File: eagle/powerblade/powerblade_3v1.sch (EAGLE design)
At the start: 94 parts, among them J1 JTAG_14PIN_IDC-NL, J21 AC_INSLOT2, J4 TC2030-JLINK-NL, Q1 2N7002, Q3 2SK1829, Q4 2SK1829, U1 TPS62122, U2 MCP6V3, U3 MSP430FR5738, U4 NRF51822QF, U6 MAX9910, U7 OPA2369, X1 16MHz, X3 32.768kHz, Y1 UREACH_XTEND

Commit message: 25 airwires
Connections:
- net GND2: now also U4.P27/AIN1/XL1
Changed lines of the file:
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@@
 <grid distance="0.1" unitdist="inch" unit="inch" style="lines" multiple="1" display="no" altdistance="0.01" altunitdist="inch" altunit="inch"/>
 <layers>
-<layer number="1" name="Top" color="4" fill="1" visible="yes" active="no"/>
-<layer number="2" name="Route2" color="1" fill="3" visible="yes" active="no"/>
-<layer number="3" name="Route3" color="4" fill="3" visible="yes" active="no"/>
-<layer number="4" name="Route4" color="1" fill="4" visible="yes" active="no"/>
-<layer number="5" name="Route5" color="4" fill="4" visible="yes" active="no"/>
-<layer number="6" name="Route6" color="1" fill="8" visible="yes" active="no"/>
-<layer number="7" name="Route7" color="4" fill="8" visible="yes" active="no"/>
-<layer number="8" name="Route8" color="1" fill="2" visible="yes" active="no"/>
-<layer number="9" name="Route9" color="4" fill="2" visible="yes" active="no"/>
-<layer number="10" name="Route10" color="1" fill="7" visible="yes" active="no"/>
-<layer number="11" name="Route11" color="4" fill="7" visible="yes" active="no"/>
-<layer number="12" name="Route12" color="1" fill="5" visible="yes" active="no"/>
-<layer number="13" name="Route13" color="4" fill="5" visible="yes" active="no"/>
-<layer number="14" name="Route14" color="1" fill="6" visible="yes" active="no"/>
-<layer number="15" name="Route15" color="4" fill="6" visible="yes" active="no"/>
-<layer number="16" name="Bottom" color="1" fill="1" visible="yes" active="no"/>
-<layer number="17" name="Pads" color="2" fill="1" visible="yes" active="no"/>
-<layer number="18" name="Vias" color="2" fill="1" visible="yes" active="no"/>
-<layer number="19" name="Unrouted" color="6" fill="1" visible="yes" active="no"/>
-<layer number="20" name="Dimension" color="15" fill="1" visible="yes" active="no"/>
-<layer number="21" name="tPlace" color="7" fill="1" visible="yes" active="no"/>
-<layer number="22" name="bPlace" color="7" fill="1" visible="yes" active="no"/>
-<layer number="23" name="tOrigins" color="15" fill="1" visible="yes" active="no"/>
-<layer number="24" name="bOrigins" color="15" fill="1" visible="yes" active="no"/>
-<layer number="25" name="tNames" color="7" fill="1" visible="yes" active="no"/>
-<layer number="26" name="bNames" color="7" fill="1" visible="yes" active="no"/>
-<layer number="27" name="tValues" color="7" fill="1" visible="yes" active="no"/>
-<layer number="28" name="bValues" color="7" fill="1" visible="yes" active="no"/>
+<layer number="1" name="Top" color="4" fill="1" visible="no" active="no"/>
+<layer number="2" name="Route2" color="1" fill="3" visible="no" active="no"/>
+<layer number="3" name="Route3" color="4" fill="3" visible="no" active="no"/>
+<layer number="4" name="Route4" color="1" fill="4" visible="no" active="no"/>
+<layer number="5" name="Route5" color="4" fill="4" visible="no" active="no"/>
+<layer number="6" name="Route6" color="1" fill="8" visible="no" active="no"/>
+<layer number="7" name="Route7" color="4" fill="8" visible="no" active="no"/>
+<layer number="8" name="Route8" color="1" fill="2" visible="no" active="no"/>
+<layer number="9" name="Route9" color="4" fill="2" visible="no" active="no"/>
+<layer number="10" name="Route10" color="1" fill="7" visible="no" active="no"/>
+<layer number="11" name="Route11" color="4" fill="7" visible="no" active="no"/>
+<layer number="12" name="Route12" color="1" fill="5" visible="no" active="no"/>
+<layer number="13" name="Route13" color="4" fill="5" visible="no" active="no"/>
+<layer number="14" name="Route14" color="1" fill="6" visible="no" active="no"/>
+<layer number="15" name="Route15" color="4" fill="6" visible="no" active="no"/>
+<layer number="16" name="Bottom" color="1" fill="1" visible="no" active="no"/>
+<layer number="17" name="Pads" color="2" fill="1" visible="no" active="no"/>
+<layer number="18" name="Vias" color="2" fill="1" visible="no" active="no"/>
+<layer number="19" name="Unrouted" color="6" fill="1" visible="no" active="no"/>
+<layer number="20" name="Dimension" color="15" fill="1" visible="no" active="no"/>
+<layer number="21" name="tPlace" color="7" fill="1" visible="no" active="no"/>
+<layer number="22" name="bPlace" color="7" fill="1" visible="no" active="no"/>
+<layer number="23" name="tOrigins" color="15" fill="1" visible="no" active="no"/>
+<layer number="24" name="bOrigins" color="15" fill="1" visible="no" active="no"/>
+<layer number="25" name="tNames" color="7" fill="1" visible="no" active="no"/>
+<layer number="26" name="bNames" color="7" fill="1" visible="no" active="no"/>
+<layer number="27" name="tValues" color="7" fill="1" visible="no" active="no"/>
+<layer number="28" name="bValues" color="7" fill="1" visible="no" active="no"/>
 <layer number="29" name="tStop" color="7" fill="3" visible="no" active="no"/>
 <layer number="30" name="bStop" color="7" fill="6" visible="no" active="no"/>
@@
 <layer number="35" name="tGlue" color="7" fill="4" visible="no" active="no"/>
 <layer number="36" name="bGlue" color="7" fill="5" visible="no" active="no"/>
-<layer number="37" name="tTest" color="7" fill="1" visible="yes" active="no"/>
-<layer number="38" name="bTest" color="7" fill="1" visible="yes" active="no"/>
+<layer number="37" name="tTest" color="7" fill="1" visible="no" active="no"/>
+<layer number="38" name="bTest" color="7" fill="1" visible="no" active="no"/>
 <layer number="39" name="tKeepout" color="4" fill="11" visible="no" active="no"/>
 <layer number="40" name="bKeepout" color="1" fill="11" visible="no" active="no"/>
@@
 <layer number="44" name="Drills" color="7" fill="1" visible="no" active="no"/>
 <layer number="45" name="Holes" color="7" fill="1" visible="no" active="no"/>
-<layer number="46" name="Milling" color="3" fill="1" visible="yes" active="no"/>
-<layer number="47" name="Measures" color="7" fill="1" visible="yes" active="no"/>
-<layer number="48" name="Document" color="7" fill="1" visible="yes" active="no"/>
-<layer number="49" name="Reference" color="7" fill="1" visible="yes" active="no"/>
-<layer number="50" name="dxf" color="7" fill="1" visible="yes" active="no"/>
-<layer number="51" name="tDocu" color="7" fill="1" visible="yes" active="no"/>
-<layer number="52" name="bDocu" color="7" fill="1" visible="yes" active="no"/>
-<layer number="53" name="tGND_GNDA" color="7" fill="9" visible="yes" active="no"/>
-<layer number="54" name="bGND_GNDA" color="1" fill="9" visible="yes" active="no"/>
-<layer number="56" name="wert" color="7" fill="1" visible="yes" active="no"/>
-<layer number="57" name="tCAD" color="7" fill="1" visible="yes" active="no"/>
+<layer number="46" name="Milling" color="3" fill="1" visible="no" active="no"/>
+<layer number="47" name="Measures" color="7" fill="1" visible="no" active="no"/>
+<layer number="48" name="Document" color="7" fill="1" visible="no" active="no"/>
+<layer number="49" name="Reference" color="7" fill="1" visible="no" active="no"/>
+<layer number="50" name="dxf" color="7" fill="1" visible="no" active="no"/>
+<layer number="51" name="tDocu" color="7" fill="1" visible="no" active="no"/>
+<layer number="52" name="bDocu" color="7" fill="1" visible="no" active="no"/>
+<layer number="53" name="tGND_GNDA" color="7" fill="9" visible="no" active="no"/>
+<layer number="54" name="bGND_GNDA" color="1" fill="9" visible="no" active="no"/>
+<layer number="56" name="wert" color="7" fill="1" visible="no" active="no"/>
+<layer number="57" name="tCAD" color="7" fill="1" visible="no" active="no"/>
 <layer number="91" name="Nets" color="2" fill="1" visible="yes" active="yes"/>
 <layer number="92" name="Busses" color="1" fill="1" visible="yes" active="yes"/>
@@
 <attribute name="DIGIKEY" value="445-5947-1-ND"/>
 </part>
+<part name="SUPPLY9" library="supply2" deviceset="GND2" device=""/>
 </parts>
 <sheets>
@@
 <attribute name="DIGIKEY" x="-63.5" y="43.18" size="1.27" layer="96" display="off"/>
 </instance>
+<instance part="SUPPLY9" gate="G$1" x="7.62" y="-12.7" rot="R90"/>
 </instances>
 <busses>
@@
 <wire x1="-10.16" y1="63.5" x2="-10.16" y2="60.96" width="0.1524" layer="91"/>
 </segment>
-</net>
+<segment>
+<pinref part="U4" gate="G$1" pin="P27/AIN1/XL1"/>
+<pinref part="SUPPLY9" gate="G$1" pin="GND2"/>
+<wire x1="-20.32" y1="-12.7" x2="5.08" y2="-12.7" width="0.1524" layer="91"/>
+</segment>
+</net>

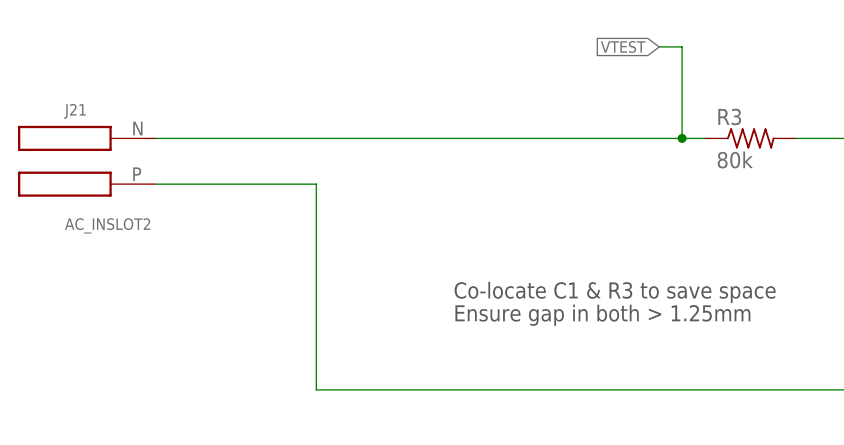
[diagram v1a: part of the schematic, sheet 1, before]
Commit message: switched phase and neutral, everything routed but 12 headers plus antenna
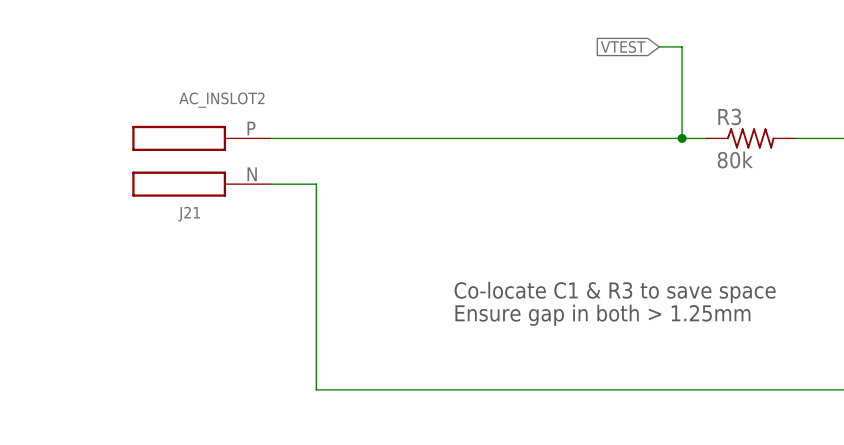
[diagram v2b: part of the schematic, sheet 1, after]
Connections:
- net GND: now also J21.P; no longer J21.N
- net VTEST: now also J21.N; no longer J21.P
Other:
- moved on the sheet: J21
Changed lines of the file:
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@@
 <instance part="GND1" gate="1" x="93.98" y="-22.86"/>
 <instance part="P+1" gate="VCC" x="93.98" y="27.94"/>
-<instance part="J21" gate="G$1" x="-58.42" y="15.24">
-<attribute name="DIGIKEY" x="-58.42" y="15.24" size="1.27" layer="96" display="off"/>
+<instance part="J21" gate="G$1" x="-45.72" y="15.24" rot="MR180">
+<attribute name="DIGIKEY" x="-45.72" y="15.24" size="1.27" layer="96" rot="MR180" display="off"/>
 </instance>
 <instance part="TP10" gate="G$1" x="121.92" y="17.78">
@@
 <segment>
 <wire x1="7.62" y1="27.94" x2="7.62" y2="17.78" width="0.1524" layer="91"/>
-<junction x="7.62" y="17.78"/>
 <wire x1="5.08" y1="27.94" x2="7.62" y2="27.94" width="0.1524" layer="91"/>
 <label x="5.08" y="27.94" size="1.27" layer="95" rot="R180" xref="yes"/>
 <pinref part="R3" gate="G$1" pin="1"/>
 <wire x1="7.62" y1="17.78" x2="10.16" y2="17.78" width="0.1524" layer="91"/>
-<pinref part="J21" gate="G$1" pin="P"/>
-<wire x1="-50.8" y1="17.78" x2="7.62" y2="17.78" width="0.1524" layer="91"/>
+<pinref part="J21" gate="G$1" pin="N"/>
+<wire x1="-38.1" y1="17.78" x2="7.62" y2="17.78" width="0.1524" layer="91"/>
+<junction x="7.62" y="17.78"/>
 </segment>
 </net>
@@
 <wire x1="104.14" y1="-10.16" x2="116.84" y2="-10.16" width="0.1524" layer="91"/>
 <wire x1="58.42" y1="-10.16" x2="58.42" y2="5.08" width="0.1524" layer="91"/>
-<pinref part="J21" gate="G$1" pin="N"/>
-<wire x1="-50.8" y1="12.7" x2="-33.02" y2="12.7" width="0.1524" layer="91"/>
 <wire x1="-33.02" y1="12.7" x2="-33.02" y2="-10.16" width="0.1524" layer="91"/>
 <wire x1="-33.02" y1="-10.16" x2="58.42" y2="-10.16" width="0.1524" layer="91"/>
@@
 <wire x1="104.14" y1="0" x2="104.14" y2="-10.16" width="0.1524" layer="91"/>
 <junction x="104.14" y="-10.16"/>
+<pinref part="J21" gate="G$1" pin="P"/>
+<wire x1="-38.1" y1="12.7" x2="-33.02" y2="12.7" width="0.1524" layer="91"/>
 </segment>
 </net>

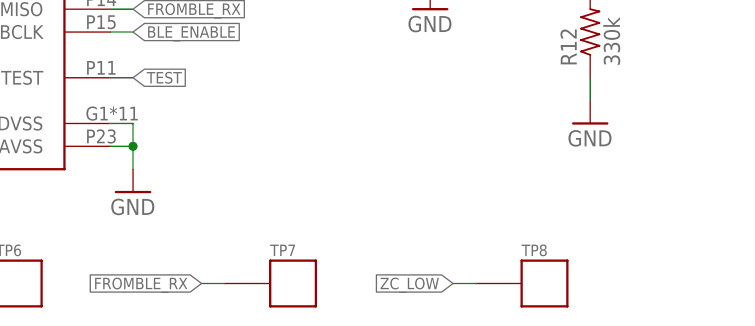
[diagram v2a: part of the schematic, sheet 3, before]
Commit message: almost done routing incl some of the headers
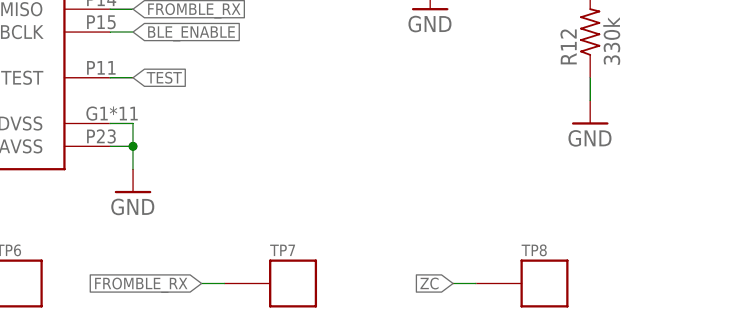
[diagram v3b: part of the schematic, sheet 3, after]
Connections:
- net ZC: now also TP8.P$1
- net ZC_LOW: no longer TP8.P$1
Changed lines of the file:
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@@
 <label x="58.42" y="25.4" size="1.27" layer="95" rot="R180" xref="yes"/>
+</segment>
+<segment>
+<pinref part="TP8" gate="G$1" pin="P$1"/>
+<wire x1="63.5" y1="-38.1" x2="66.04" y2="-38.1" width="0.1524" layer="91"/>
+<label x="63.5" y="-38.1" size="1.27" layer="95" rot="R180" xref="yes"/>
 </segment>
 </net>
@@
 <label x="27.94" y="17.78" size="1.524" layer="95"/>
 </segment>
-<segment>
-<pinref part="TP8" gate="G$1" pin="P$1"/>
-<wire x1="63.5" y1="-38.1" x2="66.04" y2="-38.1" width="0.1524" layer="91"/>
-<label x="63.5" y="-38.1" size="1.27" layer="95" rot="R180" xref="yes"/>
-</segment>
 </net>

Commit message: well... i changed to the other type of debugging connctor. not done routing
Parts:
- removed C28: 0.1uF, rcl:C-EUC0402_SM
- removed LED2: (no value), SparkFun-LED:LED0603
- removed R23: 120, rcl:R-US_R0402_SM
- removed TP10, TP11, TP12, TP3, TP4, TP5, TP6, TP7, TP8, TP9: TP_LONG, skyspecs:TP_LONG
- added C13: 0.1uF, passives:CAPACITOR
- added SV1: (no value), con-lstb:MA12-11M27
- TP1, TP2: value TP_LONG -> TP_STD; device skyspecs:TP_LONG -> skyspecs:TP_STD; DIGIKEY 5126K-ND -> (none)
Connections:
- removed net N$58: LED2.A, R23.1
- removed net N$61: C39.1, R17.2, TP2.P$1, U2.OUT
- removed net N$7: C10.1, C4.1, C9.1, L1.1, R24.1, R7.2, TP12.P$1, U1.VOUT
- new net VAMP: C39.1, R17.2, SV1.7, U2.OUT
- new net VS+: C10.1, C4.1, C9.1, L1.1, R24.1, R7.2, SV1.12, U1.VOUT
- net +3V3: now also C13.1, SV1.9, TP1.P$1; no longer C28.1, R23.2, TP11.P$1
- net FROMBLE_RX: now also SV1.2; no longer TP7.P$1
- net GND: now also SV1.11; no longer TP9.P$1
- net GND2: now also X1.GND
- net GND3: now also C13.2; no longer C28.2
- net I_SENSE: now also SV1.3; no longer TP1.P$1
- net N$59: now also TP2.P$1; no longer LED2.C
- net PWM_CURRENT: now also SV1.5; no longer TP4.P$1
- net PWM_VOLTAGE: now also SV1.6; no longer TP5.P$1
- net TOBLE_TX: now also SV1.1; no longer TP6.P$1
- net VCC: now also SV1.10; no longer TP10.P$1
- net V_SENSE: now also SV1.4; no longer TP3.P$1
- net ZC: now also SV1.8; no longer TP8.P$1

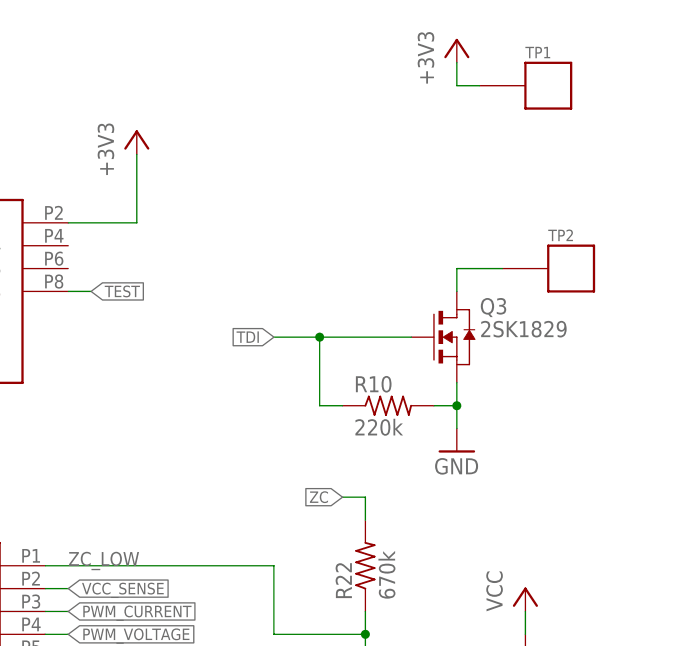
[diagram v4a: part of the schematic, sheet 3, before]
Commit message: removed led once and for all
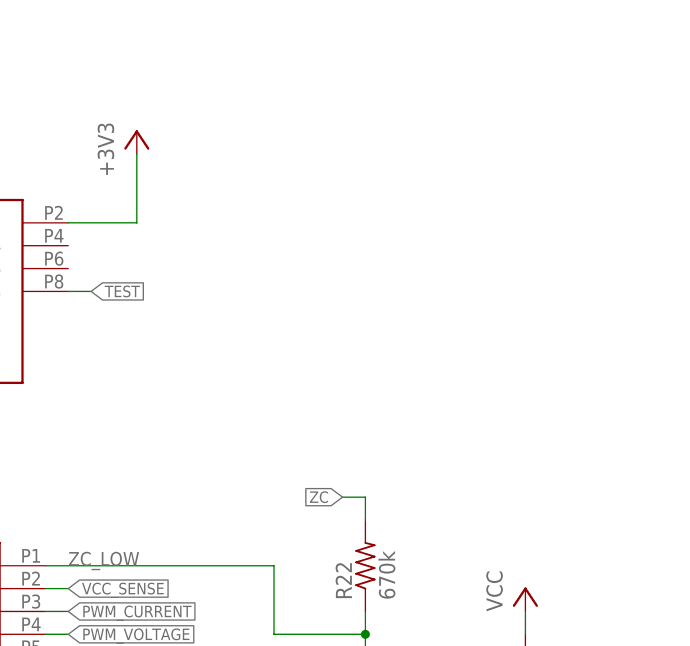
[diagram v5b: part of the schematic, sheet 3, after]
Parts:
- removed Q3: 2SK1829, powerfilm:2SK1829
- removed R10: 220k, rcl:R-US_R0402_SM
- removed TP1, TP2: TP_STD, skyspecs:TP_STD
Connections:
- removed net N$59: Q3.D, TP2.P$1
- net +3V3: no longer TP1.P$1
- net GND: no longer Q3.S, R10.2
- net TDI: no longer Q3.G, R10.1
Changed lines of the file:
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@@
 </part>
 <part name="GND26" library="supply1" deviceset="GND" device=""/>
-<part name="+3V13" library="supply1" deviceset="+3V3" device=""/>
-<part name="Q3" library="powerfilm" deviceset="2SK1829" device=""/>
-<part name="GND27" library="supply1" deviceset="GND" device=""/>
 <part name="C12" library="passives" deviceset="CAPACITOR" device="" value="1nF">
 <attribute name="DIGIKEY" value="490-1303-1-ND"/>
@@
 <part name="SUPPLY28" library="supply2" deviceset="GND3" device=""/>
 <part name="GND2" library="supply1" deviceset="GND" device=""/>
-<part name="R10" library="rcl" deviceset="R-US_" device="R0402_SM" value="220k"/>
 <part name="R13" library="rcl" deviceset="R-US_" device="R0402_SM" value="330k"/>
 <part name="R22" library="rcl" deviceset="R-US_" device="R0402_SM" value="670k"/>
@@
 <attribute name="DIGIKEY" value="445-1265-1-ND"/>
 </part>
-<part name="TP1" library="skyspecs" deviceset="TP" device="_STD"/>
-<part name="TP2" library="skyspecs" deviceset="TP" device="_STD"/>
 </parts>
 <sheets>
@@
 </instance>
 <instance part="GND26" gate="1" x="-66.04" y="-22.86"/>
-<instance part="+3V13" gate="G$1" x="71.12" y="76.2"/>
-<instance part="Q3" gate="G$1" x="71.12" y="43.18"/>
-<instance part="GND27" gate="1" x="71.12" y="30.48"/>
-<instance part="R10" gate="G$1" x="63.5" y="35.56"/>
 <instance part="R13" gate="G$1" x="60.96" y="2.54" rot="R90"/>
 <instance part="R22" gate="G$1" x="60.96" y="17.78" rot="R90"/>
 <instance part="GND8" gate="1" x="60.96" y="-7.62"/>
-<instance part="TP1" gate="G$1" x="78.74" y="71.12"/>
-<instance part="TP2" gate="G$1" x="81.28" y="50.8"/>
 </instances>
 <busses>
@@
 <wire x1="-63.5" y1="-15.24" x2="-66.04" y2="-15.24" width="0.1524" layer="91"/>
 <junction x="-66.04" y="-15.24"/>
-</segment>
-<segment>
-<pinref part="Q3" gate="G$1" pin="S"/>
-<pinref part="GND27" gate="1" pin="GND"/>
-<wire x1="71.12" y1="38.1" x2="71.12" y2="35.56" width="0.1524" layer="91"/>
-<pinref part="R10" gate="G$1" pin="2"/>
-<wire x1="71.12" y1="35.56" x2="71.12" y2="33.02" width="0.1524" layer="91"/>
-<wire x1="68.58" y1="35.56" x2="71.12" y2="35.56" width="0.1524" layer="91"/>
-<junction x="71.12" y="35.56"/>
 </segment>
 <segment>
@@
 <wire x1="27.94" y1="55.88" x2="35.56" y2="55.88" width="0.1524" layer="91"/>
 </segment>
-<segment>
-<pinref part="+3V13" gate="G$1" pin="+3V3"/>
-<wire x1="71.12" y1="73.66" x2="71.12" y2="71.12" width="0.1524" layer="91"/>
-<pinref part="TP1" gate="G$1" pin="P$1"/>
-<wire x1="73.66" y1="71.12" x2="71.12" y2="71.12" width="0.1524" layer="91"/>
-</segment>
 </net>
 <net name="RST" class="0">
@@
 <label x="5.08" y="53.34" size="1.27" layer="95" rot="R180" xref="yes"/>
 <wire x1="5.08" y1="53.34" x2="7.62" y2="53.34" width="0.1524" layer="91"/>
-</segment>
-<segment>
-<pinref part="Q3" gate="G$1" pin="G"/>
-<wire x1="50.8" y1="43.18" x2="55.88" y2="43.18" width="0.1524" layer="91"/>
-<label x="50.8" y="43.18" size="1.27" layer="95" rot="R180" xref="yes"/>
-<pinref part="R10" gate="G$1" pin="1"/>
-<wire x1="55.88" y1="43.18" x2="66.04" y2="43.18" width="0.1524" layer="91"/>
-<wire x1="58.42" y1="35.56" x2="55.88" y2="35.56" width="0.1524" layer="91"/>
-<wire x1="55.88" y1="35.56" x2="55.88" y2="43.18" width="0.1524" layer="91"/>
-<junction x="55.88" y="43.18"/>
 </segment>
 </net>
@@
 </segment>
 </net>
-<net name="N$59" class="0">
-<segment>
-<pinref part="Q3" gate="G$1" pin="D"/>
-<wire x1="71.12" y1="50.8" x2="71.12" y2="48.26" width="0.1524" layer="91"/>
-<pinref part="TP2" gate="G$1" pin="P$1"/>
-<wire x1="76.2" y1="50.8" x2="71.12" y2="50.8" width="0.1524" layer="91"/>
-</segment>
-</net>
